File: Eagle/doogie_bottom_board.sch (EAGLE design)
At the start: 31 parts, among them Q1 TEFT4300, Q2 TEFT4300, Q3 TEFT4300, Q4 TEFT4300, T1 BC337, T2 BC337, T3 BC337

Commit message: Add first version of schematics
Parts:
- removed MOTORS: SWITCHS, pololu:SWITCHS
- removed POWER: ON/OFF, pololu:SWITCHS
- removed U$2, U$3, U$4, U$5: FRAME_A4P, doogie:FRAME_A4P
- added BATTERY_HOLDER: BATTERY_HOLDER, doogie:BATTERY_HOLDER
- added J1: (no value), SparkFun-Connectors:CONN_12
- added J4: (no value), SparkFun-Connectors:CONN_03X2SHROUD
- added J5: (no value), SparkFun-Connectors:CONN_02JST-PTH-2
- added Q6: IRF9530, transistor-power:IRF9530
- added S1, S2: (no value), doogie:M9040P
- J2: device SparkFun-Connectors:CONN_03X2SHROUD -> SparkFun-Connectors:CONN_12
- Q1, Q3: device maze:TEFT4300CE -> doogie:TEFT4300_5MM_RA
- Q2, Q4: device maze:TEFT4300EC -> doogie:TEFT4300_5MM_RA
- R10, R12, R8: value 100k -> 680R
- R11: value 2R -> 33R
- R13, R9: value 7R5 -> 47R
- U1: device doogie:TB6612FNG -> pololu:TB6612FNG
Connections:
- removed net LF_EMITTER: R8.2
- removed net LF_RECEIVER: Q1.E, R4.2
- removed net L_RECEIVER: Q2.E, R5.2
- removed net MOTORAO1: J2.2, U1.AO1
- removed net MOTORAO2: J2.4, U1.AO2
- removed net N$10: J2.6
- removed net N$17: POWER.P
- removed net RF_EMITTER: R12.2
- removed net RF_RECEIVER: Q4.E, R7.2
- removed net R_RECEIVER: Q3.E, R6.2
- removed net SIDE_EMITTER: R10.2
- removed net VCC_1: U$1.IN+
- new net H-BRIDGE_!STDBY: J1.7, U1.!STDBY!
- new net LEFT_FRONT_EMITTER: J1.11, R8.2
- new net LEFT_FRONT_RCVR: J1.12, Q2.E, R5.2
- new net LEFT_RCVR: J1.5, Q1.E, R4.2
- new net LEFT_RIGHT_EMITTER: J2.4
- new net LEFT_RIGHT_EMITTERS: J1.6, R10.2
- new net MOTOR_LEFT_EN1: J1.9, U1.AIN1
- new net MOTOR_LEFT_EN2: J1.8, U1.AIN2
- new net MOTOR_LEFT_ENCA: J1.4, J3.3
- new net MOTOR_LEFT_ENCB: J1.3, J3.2
- new net MOTOR_LEFT_O1: J3.6, U1.AO1
- new net MOTOR_LEFT_O2: J3.5, U1.AO2
- new net MOTOR_LEFT_PWM: J1.10, U1.PWMA
- new net MOTOR_RIGHT_EN1: J2.6, U1.BIN1
- new net MOTOR_RIGHT_EN2: J2.5, U1.BIN2
- new net MOTOR_RIGHT_ENCA: J2.2, J4.3
- new net MOTOR_RIGHT_ENCB: J2.1, J4.2
- new net MOTOR_RIGHT_O1: J4.6, U1.BO1
- new net MOTOR_RIGHT_O2: J4.5, U1.BO2
- new net MOTOR_RIGHT_PWM: J2.7, U1.PWMB
- new net N$8: J5.2, Q6.D
- new net N$9: Q6.S, S1.P
- new net RIGHT_FRONT_EMITTER: J2.8, R12.2
- new net RIGHT_FRONT_RCVR: J2.9, Q3.E, R6.2
- new net RIGHT_RCVR: J2.3, Q4.E, R7.2
- new net VOUT: D1.A, D2.A, D4.A, J2.10, U$1.IN+, U1.VMOT
- net 3.3V: now also J2.12, J3.4, J4.4, U1.VCC; no longer D1.A, D2.A, D4.A, U$1.OUT-
- net GND: now also J1.1, J1.2, J3.1, J4.1, J5.1, Q6.G, U$1.OUT-, U1.GND@1, U1.GND@2, U1.GND@3
- net N$5: now also S2.S; no longer MOTORS.S
- net V_BATT: now also J2.11, S1.S, S2.P; no longer MOTORS.P, POWER.S
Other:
- note added: "DUAL MOTOR DRIVER"
- note added: "Doogie Mouse V1.0 by Doogie Team Licensed under CERN OHL v.1.2. http://ohwr.org/cernohl"
- note added: "LEFT MOTOR ENCODER CONNECTOR"
- note added: "RIGHT MOTOR ENCODER CONNECTOR"
- note removed: "Original drawing TON-BOT by IOTON Technology"
- note removed: "TON-BOT V1.1 - MCU, Motors and Power System"
- note removed: "TON-BOT V1.1 - Sensor System and Buzzer"
- note removed: "TON-BOT V1.1 by IOTON Technology. Licensed under CERN OHL v.1.2. http://ohwr.org/cernohl"
- note removed: "k007a"

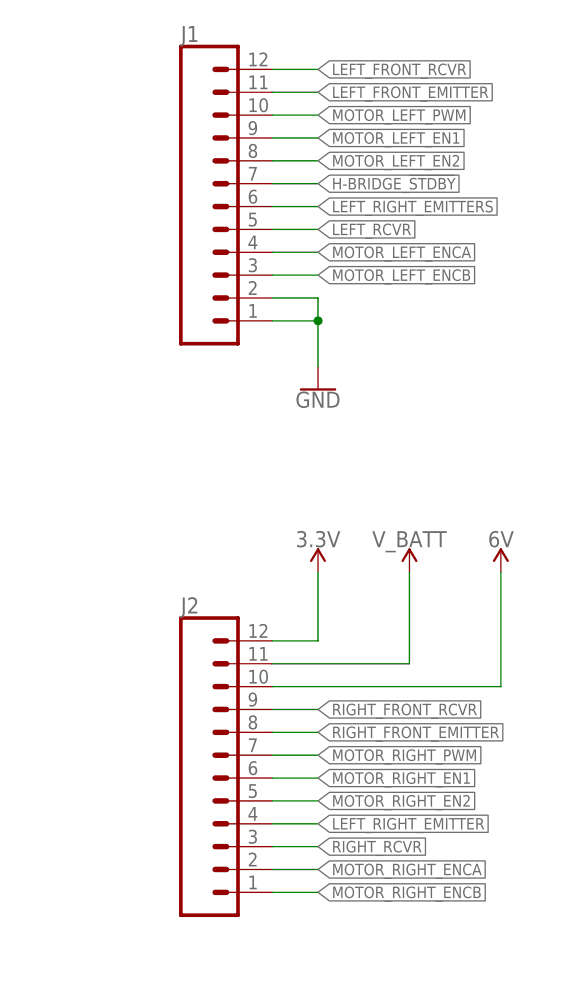
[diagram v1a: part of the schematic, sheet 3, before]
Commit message: Change net order and names
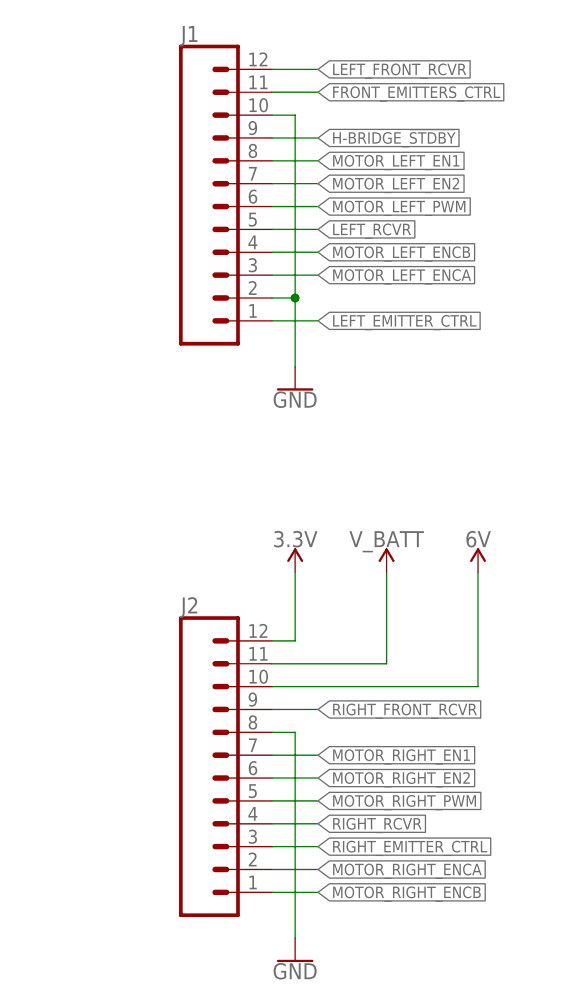
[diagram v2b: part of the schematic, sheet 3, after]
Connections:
- net VOUT renamed 6V
- removed net GND: J1.1, J1.2, J3.1, J4.1, J5.1, Q6.G, R4.1, R5.1, R6.1, R7.1, T1.E, T2.E, T3.E, U$1.IN-, U$1.OUT-, U1.GND@1, U1.GND@2, U1.GND@3
- removed net LEFT_FRONT_EMITTER: J1.11, R8.2
- removed net LEFT_RIGHT_EMITTER: J2.4
- removed net LEFT_RIGHT_EMITTERS: J1.6, R10.2
- removed net RIGHT_FRONT_EMITTER: J2.8, R12.2
- new net FILLING_POLYGON: J1.10, J1.2, J2.8, J3.1, J4.1, J5.1, Q6.G, R4.1, R5.1, R6.1, R7.1, T1.E, T2.E, T3.E, U$1.IN-, U$1.OUT-, U1.GND@1, U1.GND@2, U1.GND@3
- new net FRONT_EMITTERS_CTRL: J1.11, R10.2
- new net LEFT_EMITTER_CTRL: J1.1, R8.2
- new net RIGHT_EMITTER_CTRL: J2.3, R12.2
- net H-BRIDGE_!STDBY: now also J1.9; no longer J1.7
- net MOTOR_LEFT_EN1: now also J1.8; no longer J1.9
- net MOTOR_LEFT_EN2: now also J1.7; no longer J1.8
- net MOTOR_LEFT_ENCA: now also J1.3; no longer J1.4
- net MOTOR_LEFT_ENCB: now also J1.4; no longer J1.3
- net MOTOR_LEFT_PWM: now also J1.6; no longer J1.10
- net MOTOR_RIGHT_EN1: now also J2.7; no longer J2.6
- net MOTOR_RIGHT_EN2: now also J2.6; no longer J2.5
- net MOTOR_RIGHT_PWM: now also J2.5; no longer J2.7
- net RIGHT_RCVR: now also J2.4; no longer J2.3

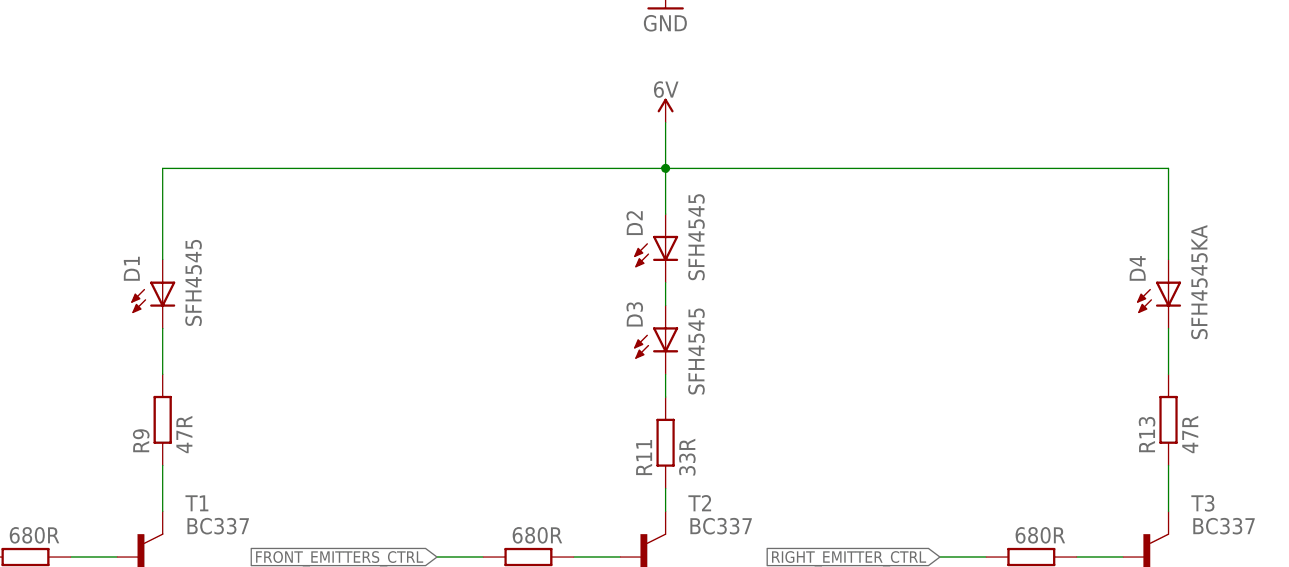
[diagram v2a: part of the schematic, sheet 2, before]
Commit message: Route bottom board
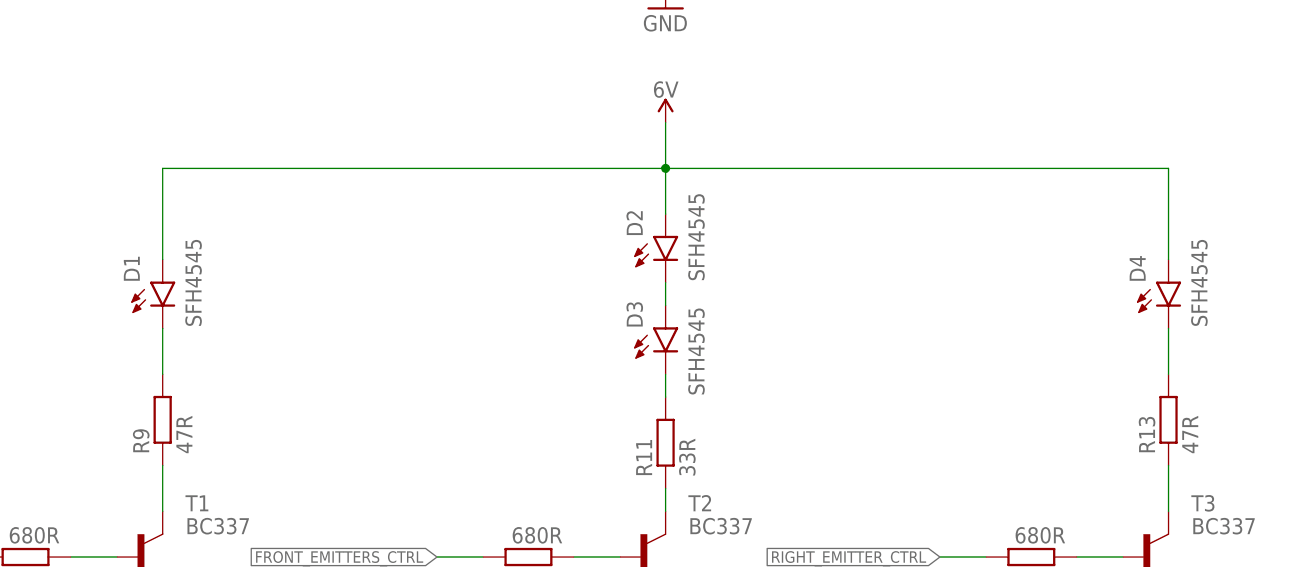
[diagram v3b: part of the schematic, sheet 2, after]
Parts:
- D1: device maze:SFH4545AK -> doogie:SFH4545
- D2, D3: device maze:SFH4545KA -> doogie:SFH4545
- D4: value SFH4545KA -> SFH4545; device maze:SFH4545KA -> doogie:SFH4545
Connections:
- net N$14: now also D2.C; no longer D2.K
- net N$15: now also D1.C; no longer D1.K
- net N$16: now also D4.C; no longer D4.K
- net N$20: now also D3.C; no longer D3.K
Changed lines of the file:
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@@
 <setting verticaltext="up"/>
 </settings>
-<grid distance="0.1" unitdist="inch" unit="inch" style="lines" multiple="1" display="yes" altdistance="0.01" altunitdist="inch" altunit="inch"/>
+<grid distance="0.1" unitdist="inch" unit="inch" style="lines" multiple="1" display="no" altdistance="0.01" altunitdist="inch" altunit="inch"/>
 <layers>
 <layer number="1" name="Top" color="4" fill="1" visible="no" active="no"/>
@@
 <layer number="16" name="Bottom" color="1" fill="1" visible="no" active="no"/>
 <layer number="17" name="Pads" color="2" fill="1" visible="no" active="no"/>
-<layer number="18" name="Vias" color="2" fill="1" visible="no" active="no"/>
+<layer number="18" name="Vias" color="14" fill="1" visible="no" active="no"/>
 <layer number="19" name="Unrouted" color="6" fill="1" visible="no" active="no"/>
 <layer number="20" name="Dimension" color="15" fill="1" visible="no" active="no"/>
@@
 <layer number="50" name="dxf" color="7" fill="1" visible="no" active="no"/>
 <layer number="51" name="tDocu" color="14" fill="1" visible="no" active="no"/>
-<layer number="52" name="bDocu" color="7" fill="1" visible="no" active="no"/>
+<layer number="52" name="bDocu" color="6" fill="1" visible="no" active="no"/>
 <layer number="53" name="tGND_GNDA" color="7" fill="9" visible="no" active="no"/>
 <layer number="54" name="bGND_GNDA" color="1" fill="9" visible="no" active="no"/>
@@
 </classes>
 <parts>
-<part name="D1" library="maze" deviceset="SFH4545" device="AK" value="SFH4545"/>
-<part name="D4" library="maze" deviceset="SFH4545" device="KA" value="SFH4545KA"/>
+<part name="D1" library="doogie" deviceset="SFH4545" device="" value="SFH4545"/>
+<part name="D4" library="doogie" deviceset="SFH4545" device="" value="SFH4545"/>
 <part name="Q1" library="doogie" deviceset="TEFT4300_5MM_RA" device="" value="TEFT4300"/>
 <part name="Q4" library="doogie" deviceset="TEFT4300_5MM_RA" device="" value="TEFT4300"/>
-<part name="D2" library="maze" deviceset="SFH4545" device="KA" value="SFH4545"/>
-<part name="D3" library="maze" deviceset="SFH4545" device="KA" value="SFH4545"/>
+<part name="D2" library="doogie" deviceset="SFH4545" device="" value="SFH4545"/>
+<part name="D3" library="doogie" deviceset="SFH4545" device="" value="SFH4545"/>
 <part name="Q2" library="doogie" deviceset="TEFT4300_5MM_RA" device="" value="TEFT4300"/>
 <part name="Q3" library="doogie" deviceset="TEFT4300_5MM_RA" device="" value="TEFT4300"/>
@@
 <net name="N$15" class="0">
 <segment>
-<pinref part="D1" gate="G$1" pin="K"/>
+<pinref part="D1" gate="G$1" pin="C"/>
 <pinref part="R9" gate="G$1" pin="2"/>
 <wire x1="73.66" y1="78.74" x2="73.66" y2="83.82" width="0.1524" layer="91"/>
@@
 <net name="N$16" class="0">
 <segment>
-<pinref part="D4" gate="G$1" pin="K"/>
+<pinref part="D4" gate="G$1" pin="C"/>
 <pinref part="R13" gate="G$1" pin="2"/>
 <wire x1="185.42" y1="78.74" x2="185.42" y2="83.82" width="0.1524" layer="91"/>
@@
 <segment>
 <pinref part="D3" gate="G$1" pin="A"/>
-<pinref part="D2" gate="G$1" pin="K"/>
+<pinref part="D2" gate="G$1" pin="C"/>
 <wire x1="129.54" y1="88.9" x2="129.54" y2="86.36" width="0.1524" layer="91"/>
 </segment>
@@
 <segment>
 <pinref part="R11" gate="G$1" pin="2"/>
-<pinref part="D3" gate="G$1" pin="K"/>
+<pinref part="D3" gate="G$1" pin="C"/>
 <wire x1="129.54" y1="78.74" x2="129.54" y2="76.2" width="0.1524" layer="91"/>
 </segment>

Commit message: Add H-bridge name on bottom board silk
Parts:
- U1: value (none) -> TB6612FNG; device pololu:TB6612FNG -> doogie:TB6612FNG
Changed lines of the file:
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@@
 <part name="GND13" library="SparkFun-PowerSymbols" library_urn="urn:adsk.eagle:library:530" deviceset="GND" device=""/>
 <part name="SUPPLY11" library="SparkFun-PowerSymbols" library_urn="urn:adsk.eagle:library:530" deviceset="3.3V" device=""/>
-<part name="U1" library="pololu" deviceset="TB6612FNG" device=""/>
+<part name="U1" library="doogie" deviceset="TB6612FNG" device="" value="TB6612FNG"/>
 <part name="GND8" library="SparkFun-PowerSymbols" library_urn="urn:adsk.eagle:library:530" deviceset="GND" device=""/>
 <part name="GND9" library="SparkFun-PowerSymbols" library_urn="urn:adsk.eagle:library:530" deviceset="GND" device=""/>
